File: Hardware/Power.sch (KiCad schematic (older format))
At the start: 6 parts, among them U2 LM1117-3.3

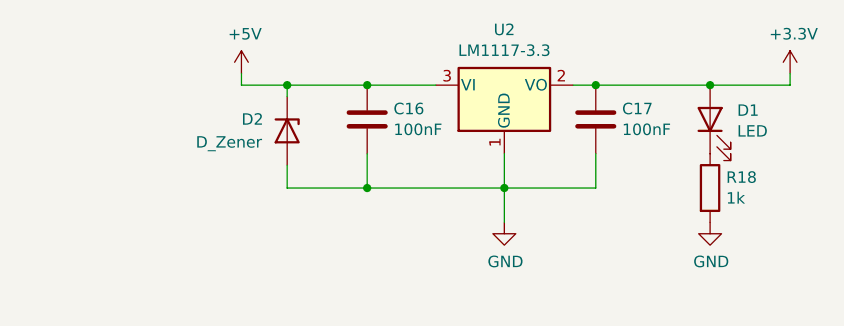
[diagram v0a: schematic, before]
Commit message: added fuse
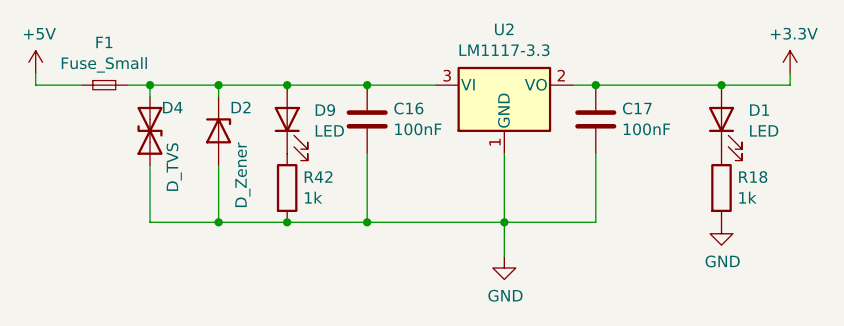
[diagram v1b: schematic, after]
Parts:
- added D4: D_TVS, Diode_SMD:D_1210_3225Metric, symbol Device:D_TVS
- added D9: LED, Diode_SMD:D_0805_2012Metric_Castellated, symbol Device:LED
- added F1: Fuse_Small, symbol Device:Fuse_Small
- added R42: 1k, Resistor_SMD:R_0603_1608Metric, symbol Device:R
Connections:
- net +5V: now also F1.1; no longer C16.1, D2.1 (K), U2.3 (VI)
- net GND: now also D4.1 (A1), R42.2
- new net: C16.1, D2.1 (K), D4.2 (A2), D9.2 (A), F1.2, U2.3 (VI)
- new net: D9.1 (K), R42.1
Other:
- moved on the sheet: D1, D2, R18
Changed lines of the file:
@@
 $EndComp
 Wire Wire Line
-	5000 3600 4700 3600
-Wire Wire Line
-	4700 3900 4700 4050
-Wire Wire Line
-	5300 4050 5300 3900
-Wire Wire Line
-	5700 3900 5700 4050
-Connection ~ 5300 4050
-Wire Wire Line
-	5300 4050 5300 4200
+	5300 4200 5300 4350
 $Comp
 L power:GND #PWR025
 U 1 1 61AB651C
-P 5300 4200
-F 0 "#PWR025" H 5300 3950 50  0001 C CNN
-F 1 "GND" H 5305 4027 50  0000 C CNN
-F 2 "" H 5300 4200 50  0001 C CNN
-F 3 "" H 5300 4200 50  0001 C CNN
-	1    5300 4200
+P 5300 4350
+F 0 "#PWR025" H 5300 4100 50  0001 C CNN
+F 1 "GND" H 5305 4177 50  0000 C CNN
+F 2 "" H 5300 4350 50  0001 C CNN
+F 3 "" H 5300 4350 50  0001 C CNN
+	1    5300 4350
 	1    0    0    -1
 $EndComp
@@
 L power:+5V #PWR023
 U 1 1 61AB7127
-P 4150 3550
-F 0 "#PWR023" H 4150 3400 50  0001 C CNN
-F 1 "+5V" H 4165 3723 50  0000 C CNN
-F 2 "" H 4150 3550 50  0001 C CNN
-F 3 "" H 4150 3550 50  0001 C CNN
-	1    4150 3550
+P 3250 3550
+F 0 "#PWR023" H 3250 3400 50  0001 C CNN
+F 1 "+5V" H 3265 3723 50  0000 C CNN
+F 2 "" H 3250 3550 50  0001 C CNN
+F 3 "" H 3250 3550 50  0001 C CNN
+	1    3250 3550
 	1    0    0    -1
 $EndComp
@@
 	1    0    0    -1
 $EndComp
-Wire Wire Line
-	4150 3550 4150 3600
 $Comp
 L Device:D_Zener D2
 U 1 1 61ABC565
-P 4350 3800
-F 0 "D2" V 4300 3600 50  0000 L CNN
-F 1 "D_Zener" V 4400 3400 50  0000 L CNN
-F 2 "Diode_SMD:D_SMB" H 4350 3800 50  0001 C CNN
-F 3 "~" H 4350 3800 50  0001 C CNN
-	1    4350 3800
+P 4050 3800
+F 0 "D2" V 3950 3850 50  0000 L CNN
+F 1 "D_Zener" H 4100 3900 50  0000 L CNN
+F 2 "Diode_SMD:D_SMB" H 4050 3800 50  0001 C CNN
+F 3 "~" H 4050 3800 50  0001 C CNN
+	1    4050 3800
 	0    1    1    0
 $EndComp
-Wire Wire Line
-	4350 3650 4350 3600
-Connection ~ 4350 3600
-Wire Wire Line
-	4350 3950 4350 4050
 $Comp
 L Device:LED D1
 U 1 1 61AC0656
-P 6200 3750
-F 0 "D1" V 6239 3632 50  0000 R CNN
-F 1 "LED" V 6148 3632 50  0000 R CNN
-F 2 "Diode_SMD:D_0805_2012Metric_Castellated" H 6200 3750 50  0001 C CNN
-F 3 "~" H 6200 3750 50  0001 C CNN
-	1    6200 3750
+P 6250 3750
+F 0 "D1" V 6289 3632 50  0000 R CNN
+F 1 "LED" V 6198 3632 50  0000 R CNN
+F 2 "Diode_SMD:D_0805_2012Metric_Castellated" H 6250 3750 50  0001 C CNN
+F 3 "~" H 6250 3750 50  0001 C CNN
+	1    6250 3750
 	0    -1   -1   0
 $EndComp
@@
 L Device:R R18
 U 1 1 61AC2812
-P 6200 4050
-F 0 "R18" H 6270 4096 50  0000 L CNN
-F 1 "1k" H 6270 4005 50  0000 L CNN
-F 2 "Resistor_SMD:R_0603_1608Metric" V 6130 4050 50  0001 C CNN
-F 3 "~" H 6200 4050 50  0001 C CNN
-	1    6200 4050
+P 6250 4050
+F 0 "R18" H 6320 4096 50  0000 L CNN
+F 1 "1k" H 6320 4005 50  0000 L CNN
+F 2 "Resistor_SMD:R_0603_1608Metric" V 6180 4050 50  0001 C CNN
+F 3 "~" H 6250 4050 50  0001 C CNN
+	1    6250 4050
 	1    0    0    -1
 $EndComp
@@
 L power:GND #PWR026
 U 1 1 61AC3D3A
-P 6200 4200
-F 0 "#PWR026" H 6200 3950 50  0001 C CNN
-F 1 "GND" H 6205 4027 50  0000 C CNN
-F 2 "" H 6200 4200 50  0001 C CNN
-F 3 "" H 6200 4200 50  0001 C CNN
-	1    6200 4200
+P 6250 4200
+F 0 "#PWR026" H 6250 3950 50  0001 C CNN
+F 1 "GND" H 6255 4027 50  0000 C CNN
+F 2 "" H 6250 4200 50  0001 C CNN
+F 3 "" H 6250 4200 50  0001 C CNN
+	1    6250 4200
 	1    0    0    -1
 $EndComp
-Connection ~ 4700 3600
-Connection ~ 4700 4050
-Wire Wire Line
-	4700 4050 5300 4050
-Wire Wire Line
-	4350 4050 4700 4050
-Wire Wire Line
-	4350 3600 4700 3600
 Connection ~ 5700 3600
 Wire Wire Line
 	5700 3600 5600 3600
+$Comp
+L Device:Fuse_Small F1
+U 1 1 62AAC622
+P 3550 3600
+F 0 "F1" H 3550 3785 50  0000 C CNN
+F 1 "Fuse_Small" H 3550 3694 50  0000 C CNN
+F 2 "" H 3550 3600 50  0001 C CNN
+F 3 "~" H 3550 3600 50  0001 C CNN
+	1    3550 3600
+	1    0    0    -1
+$EndComp
 Wire Wire Line
-	5700 4050 5300 4050
+	3250 3600 3250 3550
 Wire Wire Line
-	5700 3600 6200 3600
-Connection ~ 6200 3600
+	3450 3600 3250 3600
 Wire Wire Line
-	6200 3600 6550 3600
+	3750 3600 3750 3650
+$Comp
+L Device:D_TVS D?
+U 1 1 62AB5DAA
+P 3750 3800
+AR Path="/62AB5DAA" Ref="D?"  Part="1"
+AR Path="/61A6380E/62AB5DAA" Ref="D4"  Part="1"
+F 0 "D4" V 3850 3750 50  0000 R CNN
+F 1 "D_TVS" H 3700 3700 50  0000 R CNN
+F 2 "Diode_SMD:D_1210_3225Metric" H 3750 3800 50  0001 C CNN
+F 3 "https://www.tme.eu/Document/480040166f76761f76124a50403ca5aa/esd3b5v0ws.pdf" H 3750 3800 50  0001 C CNN
+	1    3750 3800
+	0    -1   -1   0
+$EndComp
 Wire Wire Line
-	4150 3600 4350 3600
+	5700 3600 6250 3600
+Connection ~ 6250 3600
+Wire Wire Line
+	6250 3600 6550 3600
+$Comp
+L Device:LED D9
+U 1 1 62ABFDE6
+P 4350 3750
+F 0 "D9" V 4389 3632 50  0000 R CNN
+F 1 "LED" V 4298 3632 50  0000 R CNN
+F 2 "Diode_SMD:D_0805_2012Metric_Castellated" H 4350 3750 50  0001 C CNN
+F 3 "~" H 4350 3750 50  0001 C CNN
+	1    4350 3750
+	0    -1   -1   0
+$EndComp
+$Comp
+L Device:R R42
+U 1 1 62ABFDEC
+P 4350 4050
+F 0 "R42" H 4420 4096 50  0000 L CNN
+F 1 "1k" H 4420 4005 50  0000 L CNN
+F 2 "Resistor_SMD:R_0603_1608Metric" V 4280 4050 50  0001 C CNN
+F 3 "~" H 4350 4050 50  0001 C CNN
+	1    4350 4050
+	1    0    0    -1
+$EndComp
+Wire Wire Line
+	4050 3600 4050 3650
+Connection ~ 4050 3600
+Wire Wire Line
+	4050 3600 4350 3600
+Connection ~ 4350 3600
+Wire Wire Line
+	4350 3600 4700 3600
+Connection ~ 4350 4200
+Wire Wire Line
+	4350 4200 4700 4200
+Wire Wire Line
+	5700 3900 5700 4200
+Wire Wire Line
+	5300 3900 5300 4200
+Connection ~ 5300 4200
+Wire Wire Line
+	5300 4200 5700 4200
+Wire Wire Line
+	4700 3900 4700 4200
+Connection ~ 4700 4200
+Wire Wire Line
+	4700 4200 5300 4200
+Wire Wire Line
+	4050 3950 4050 4200
+Connection ~ 4050 4200
+Wire Wire Line
+	4050 4200 4350 4200
+Wire Wire Line
+	3750 3950 3750 4200
+Connection ~ 3750 3600
+Wire Wire Line
+	3750 3600 3650 3600
+Wire Wire Line
+	3750 3600 4050 3600
+Wire Wire Line
+	3750 4200 4050 4200
+Wire Wire Line
+	5000 3600 4700 3600
+Connection ~ 4700 3600
 $EndSCHEMATC

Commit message: updated pcb
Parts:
- F1: footprint (none) -> Fuse:Fuse_1206_3216Metric
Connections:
- net safe5V: now reaches C16.1, D2.1 (K), D4.2 (A2), D9.2 (A), F1.2, U2.3 (VI)
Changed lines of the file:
@@
 F 0 "F1" H 3550 3785 50  0000 C CNN
 F 1 "Fuse_Small" H 3550 3694 50  0000 C CNN
-F 2 "" H 3550 3600 50  0001 C CNN
+F 2 "Fuse:Fuse_1206_3216Metric" H 3550 3600 50  0001 C CNN
 F 3 "~" H 3550 3600 50  0001 C CNN
 	1    3550 3600
@@
 Wire Wire Line
 	4050 3600 4050 3650
-Connection ~ 4050 3600
-Wire Wire Line
-	4050 3600 4350 3600
-Connection ~ 4350 3600
 Wire Wire Line
 	4350 3600 4700 3600
@@
 	5000 3600 4700 3600
 Connection ~ 4700 3600
+Text GLabel 4400 3400 2    50   Input ~ 0
+safe5V
+Wire Wire Line
+	4350 3400 4400 3400
+Wire Wire Line
+	4050 3600 4350 3600
+Connection ~ 4050 3600
+Connection ~ 4350 3600
+Wire Wire Line
+	4350 3400 4350 3600
 $EndSCHEMATC
